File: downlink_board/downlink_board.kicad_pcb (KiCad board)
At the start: 2 copper layers, 65 x 56 mm, 56 parts, among them J1 USB_C_Receptacle_USB2.0, J2 SCREEN, J3 GPIO, J4 PROGRAM, SW1 RPi_{ON}, SW2 RPi_{OFF}, SW3 MCU_{RST}, U1 AZ1117-3.3, U2 TPS563208DDCR, U3 STM32F103C8Tx, U4 nRF24L01, Y1 8M

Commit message: Completed Rev 1.0 layout
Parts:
- removed the C2 at (-5.35, 80.5)
- BT1: moved to F.Cu
- C1: value 22u -> 10u
- C3: renamed from C4; value 22u -> 100n; footprint Capacitor_SMD:C_0805_2012Metric -> Capacitor_SMD:C_0603_1608Metric
- J4: footprint Connector_PinSocket_2.54mm:PinSocket_1x03_P2.54mm_Vertical -> Connector_PinHeader_2.54mm:PinHeader_1x03_P2.54mm_Vertical
- moved R6 155.4 mm to (128.5, 72.2)
- moved U2 154.4 mm to (124.0, 72.2), turned to 0 degrees
- moved R7 148.9 mm to (127.0, 72.2)
- moved R5 148.3 mm to (124.0, 74.8), turned to 0 degrees
- moved C5 136.3 mm to (124.5, 69.5), turned to 180 degrees
- moved JP1 129.9 mm to (154.2, 75.0), turned to 180 degrees
- moved L1 128.9 mm to (111.6, 69.7), turned to 90 degrees
- moved C3 126.7 mm to (118.1, 72.2)
- moved D2 125.1 mm to (107.0, 68.1), turned to 90 degrees
- moved U4 123.0 mm to (125.2, 58.2), turned to 0 degrees
- moved U1 121.5 mm to (151.5, 84.5)
- moved C1 118.8 mm to (116.2, 72.2)
- moved C7 116.7 mm to (116.6, 67.2), turned to 180 degrees
- moved C4 116.2 mm to (146.0, 82.8), turned to -90 degrees
- moved R10 115.6 mm to (107.0, 71.7), turned to 90 degrees
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- renumbered C11 to C10, C12 to C11, C13 to C12, C14 to C13, C15 to C14, C16 to C15, C3 to C2, C5 to C4, C6 to C5, C7 to C6, C8 to C7, C9 to C8, C10 to C9
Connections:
- U3 pad 10: /BATT_{DIV} -> unconnected-(U3-PA0-Pad10)
- U3 pad 12: unconnected-(U3-PA2-Pad12) -> /RF_{EN}
- U3 pad 13: unconnected-(U3-PA3-Pad13) -> /RF_{SEL}
- U3 pad 14: /RF_{INT} -> unconnected-(U3-PA4-Pad14)
- U3 pad 18: /RF_{SEL} -> /RF_{INT}
- U3 pad 19: /RF_{EN} -> /BATT_{DIV}
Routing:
- net /GPIO26: track 0.00 -> 94.5 mm
- net /RST_{MCU}: track 0.00 -> 63.9 mm, vias 0 -> 1
- net /SCL: track 0.00 -> 60.5 mm
- net /RPi_{TX}: track 0.00 -> 51.7 mm, vias 0 -> 3
- net /RPi_{RX}: track 0.00 -> 43.0 mm, vias 0 -> 3
- net /USB_D-: track 0.00 -> 26.9 mm
- net /USB_D+: track 0.00 -> 26.9 mm
- net /BATT_{DIV}: track 0.00 -> 23.9 mm, vias 0 -> 2
- net /STATUS_{3}: track 0.00 -> 19.0 mm, vias 0 -> 2
- net Net-(U1-VI): track 0.00 -> 18.8 mm
- net Net-(JP1-A): track 0.00 -> 18.6 mm
- net /RF_{EN}: track 0.00 -> 17.3 mm
- net unconnected-(J1-SHIELD-PadS1): track 0.00 -> 17.0 mm
- net /MISO: track 0.00 -> 16.9 mm, vias 0 -> 1
- net +3.3V: track 0.00 -> 16.0 mm, vias 0 -> 5
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- added copper zone on B.Cu, net +3.3V
- added copper zone on F.Cu, net +5V
- added copper zone on F.Cu, net +BATT
- added copper zone on F.Cu, net GND
- added copper zone on B.Cu, net Net-(U2-SW)
- added copper zone on F.Cu, net Net-(U2-SW)
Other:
- board text added: "+BATT COVERS THIS TEXT"
- board text added: "3V3"
- board text added: "5V"
- board text added: "5V ON"
- board text added: "BOOT0"
- board text added: "GND"
- board text added: "GND COVERS THIS TEXT"
- board text added: "HPVDT GENERAL DOWNLINK"
- board text added: "MCU RST"
- board text added: "MEANT FOR TOUCHSCREEN"
- board text added: "ONLY CONNECT USB PWR WHEN RPi IS ABSENT!!"
- board text added: "R: ${REVISION}"
- board text added: "RPi OFF"
- board text added: "RPi ON"
- board text added: "SCL"
- board text added: "SDA"
- board text added: "STAT1"
- board text added: "STAT2"
- board text added: "STAT3"
- board text added: "SWCLK"
- board text added: "SWDIO"
- board text added: "The voltage regulator layout is a bit wonky but it's following TI recommendations"
- board text added: "USB PWR"
- board text added: "nRF24L01 COVER THIS"

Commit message: Layout Rev 1.1
Added a keepout area under where the antenna header will go to ensure that if it scratches the board no shorts will occur.
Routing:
- net /STATUS_{3}: track 19.0 -> 20.4 mm
- net /STATUS_{2}: track 15.1 -> 16.1 mm
- net /STATUS_{1}: track 12.2 -> 12.9 mm
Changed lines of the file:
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@@
     (title "Downlink")
     (date "2023-12-05")
-    (rev "1.0")
+    (rev "1.1")
     (company "HPVDT")
     (comment 1 "Common downlink board")
@@
     (effects (font (size 2 2) (thickness 0.15)))
   )
-  (gr_text "The voltage regulator layout is a bit wonky but it's following TI recommendations" (at 101.4 107.6) (layer "User.1")
+  (gr_text "The voltage regulator layout is a bit wonky but it's following TI recommendations" (at 101.4 107.6) (layer "Cmts.User")
     (effects (font (size 1 1) (thickness 0.15)) (justify left bottom))
   )
@@
       (effects (font (size 1 1) (thickness 0.15)) (justify left top mirror))
   )
+  (gr_text_box "Prevent scratches from antenna shorting things"
+    (start 154.5 57.4) (end 165 66.4) (layer "Cmts.User")
+      (effects (font (size 1 1) (thickness 0.15) italic) (justify left top))
+  )
   (segment (start 110.91 55.16) (end 111 55.25) (width 0.25) (layer "B.Cu") (net 2))
   (segment (start 110.91 48.77) (end 110.91 55.16) (width 0.25) (layer "B.Cu") (net 2))
@@
   (segment (start 128.75 74.75) (end 134 69.5) (width 0.25) (layer "B.Cu") (net 15))
   (segment (start 157.25 74.675) (end 157.25 73.1875) (width 0.25) (layer "F.Cu") (net 16))
+  (segment (start 150.6 64.2) (end 150.2 63.8) (width 0.25) (layer "F.Cu") (net 17))
   (segment (start 148.6625 63.25) (end 149.65 63.25) (width 0.25) (layer "F.Cu") (net 17))
-  (segment (start 149.65 63.25) (end 151.2 64.8) (width 0.25) (layer "F.Cu") (net 17))
-  (via (at 151.2 64.8) (size 0.8) (drill 0.4) (layers "F.Cu" "B.Cu") (net 17))
+  (segment (start 149.65 63.25) (end 150.2 63.8) (width 0.25) (layer "F.Cu") (net 17))
+  (segment (start 150.6 65.8) (end 150.6 64.2) (width 0.25) (layer "F.Cu") (net 17))
   (via (at 157.25 71.3125) (size 0.8) (drill 0.4) (layers "F.Cu" "B.Cu") (net 17))
-  (segment (start 157.25 70.85) (end 157.25 71.3125) (width 0.25) (layer "B.Cu") (net 17))
-  (segment (start 151.2 64.8) (end 157.25 70.85) (width 0.25) (layer "B.Cu") (net 17))
+  (via (at 150.6 65.8) (size 0.8) (drill 0.4) (layers "F.Cu" "B.Cu") (net 17))
+  (segment (start 157.25 71.3125) (end 156.1125 71.3125) (width 0.25) (layer "B.Cu") (net 17))
+  (segment (start 156.1125 71.3125) (end 150.6 65.8) (width 0.25) (layer "B.Cu") (net 17))
   (segment (start 107 70.85) (end 107 69.085) (width 0.25) (layer "F.Cu") (net 18))
-  (segment (start 150.376996 62.75) (end 152.426996 64.8) (width 0.25) (layer "F.Cu") (net 19))
+  (segment (start 151.4 63.773004) (end 150.376996 62.75) (width 0.25) (layer "F.Cu") (net 19))
   (segment (start 148.6625 62.75) (end 150.376996 62.75) (width 0.25) (layer "F.Cu") (net 19))
+  (segment (start 151.4 65) (end 151.4 63.773004) (width 0.25) (layer "F.Cu") (net 19))
   (via (at 160.25 71.3125) (size 0.8) (drill 0.4) (layers "F.Cu" "B.Cu") (net 19))
-  (via (at 152.426996 64.8) (size 0.8) (drill 0.4) (layers "F.Cu" "B.Cu") (net 19))
-  (segment (start 153.7375 64.8) (end 160.25 71.3125) (width 0.25) (layer "B.Cu") (net 19))
-  (segment (start 152.426996 64.8) (end 153.7375 64.8) (width 0.25) (layer "B.Cu") (net 19))
+  (via (at 151.4 65) (size 0.8) (drill 0.4) (layers "F.Cu" "B.Cu") (net 19))
+  (segment (start 156.4 70.4) (end 151.4 65.4) (width 0.25) (layer "B.Cu") (net 19))
+  (segment (start 159 71.3125) (end 158.0875 70.4) (width 0.25) (layer "B.Cu") (net 19))
+  (segment (start 158.939496 71.3125) (end 159 71.3125) (width 0.25) (layer "B.Cu") (net 19))
+  (segment (start 159 71.3125) (end 160.25 71.3125) (width 0.25) (layer "B.Cu") (net 19))
+  (segment (start 151.4 65.4) (end 151.4 65) (width 0.25) (layer "B.Cu") (net 19))
+  (segment (start 158.0875 70.4) (end 156.4 70.4) (width 0.25) (layer "B.Cu") (net 19))
   (segment (start 160.25 74.675) (end 160.25 73.1875) (width 0.25) (layer "F.Cu") (net 20))
   (segment (start 148.6625 61.75) (end 150.176996 61.75) (width 0.25) (layer "F.Cu") (net 21))
+  (segment (start 150.501996 61.425) (end 151.498004 61.425) (width 0.25) (layer "F.Cu") (net 21))
+  (segment (start 152.2 62.126996) (end 152.2 64.2) (width 0.25) (layer "F.Cu") (net 21))
+  (segment (start 151.498004 61.425) (end 152.2 62.126996) (width 0.25) (layer "F.Cu") (net 21))
   (segment (start 150.176996 61.75) (end 150.501996 61.425) (width 0.25) (layer "F.Cu") (net 21))
-  (segment (start 150.501996 61.425) (end 153.825 61.425) (width 0.25) (layer "F.Cu") (net 21))
-  (segment (start 153.825 61.425) (end 157.2 64.8) (width 0.25) (layer "F.Cu") (net 21))
-  (via (at 157.2 64.8) (size 0.8) (drill 0.4) (layers "F.Cu" "B.Cu") (net 21))
+  (via (at 152.2 64.2) (size 0.8) (drill 0.4) (layers "F.Cu" "B.Cu") (net 21))
   (via (at 163.0255 71.3125) (size 0.8) (drill 0.4) (layers "F.Cu" "B.Cu") (net 21))
-  (segment (start 157.2 64.8) (end 163.0255 70.6255) (width 0.25) (layer "B.Cu") (net 21))
-  (segment (start 163.0255 70.6255) (end 163.0255 71.3125) (width 0.25) (layer "B.Cu") (net 21))
+  (segment (start 152.2 65.2) (end 152.2 64.2) (width 0.25) (layer "B.Cu") (net 21))
+  (segment (start 160.2 69.8) (end 156.8 69.8) (width 0.25) (layer "B.Cu") (net 21))
+  (segment (start 163.0255 71.3125) (end 161.7125 71.3125) (width 0.25) (layer "B.Cu") (net 21))
+  (segment (start 161.7125 71.3125) (end 160.2 69.8) (width 0.25) (layer "B.Cu") (net 21))
+  (segment (start 156.8 69.8) (end 152.2 65.2) (width 0.25) (layer "B.Cu") (net 21))
   (segment (start 144.75 67.1625) (end 144.75 65.85) (width 0.25) (layer "F.Cu") (net 22))
   (segment (start 142.6 50.2) (end 142.6 52.8) (width 0.25) (layer "F.Cu") (net 22))
@@
   (segment (start 144.25 60.25) (end 145.8 61.8) (width 0.25) (layer "F.Cu") (net 32))
   (via (at 145.8 61.8) (size 0.8) (drill 0.4) (layers "F.Cu" "B.Cu") (net 32))
+  (segment (start 145.8 61.8) (end 146.875 62.875) (width 0.25) (layer "B.Cu") (net 32))
   (segment (start 161.75 92.25) (end 157.5 92.25) (width 0.25) (layer "B.Cu") (net 32))
-  (segment (start 163.75 90.25) (end 161.75 92.25) (width 0.25) (layer "B.Cu") (net 32))
-  (segment (start 147.75 63.75) (end 158.25 63.75) (width 0.25) (layer "B.Cu") (net 32))
+  (segment (start 146.875 62.875) (end 157.375 62.875) (width 0.25) (layer "B.Cu") (net 32))
+  (segment (start 157.375 62.875) (end 163.75 69.25) (width 0.25) (layer "B.Cu") (net 32))
   (segment (start 163.75 69.25) (end 163.75 90.25) (width 0.25) (layer "B.Cu") (net 32))
   (segment (start 157.5 92.25) (end 156 93.75) (width 0.25) (layer "B.Cu") (net 32))
-  (segment (start 145.8 61.8) (end 147.75 63.75) (width 0.25) (layer "B.Cu") (net 32))
   (segment (start 149.5 93.75) (end 156 93.75) (width 0.25) (layer "B.Cu") (net 32))
-  (segment (start 158.25 63.75) (end 163.75 69.25) (width 0.25) (layer "B.Cu") (net 32))
+  (segment (start 163.75 90.25) (end 161.75 92.25) (width 0.25) (layer "B.Cu") (net 32))
   (segment (start 145 87.851166) (end 144.875 87.726166) (width 0.4) (layer "F.Cu") (net 33))
   (segment (start 144.45 92.19) (end 145 91.64) (width 0.4) (layer "F.Cu") (net 33))
@@
       )
     )
+  )
+  (zone (net 0) (net_name "") (layer "F.Cu") (name "ANTENNA") (hatch edge 0.5)
+    (connect_pads (clearance 0))
+    (min_thickness 0.25) (filled_areas_thickness no)
+    (keepout (tracks not_allowed) (vias not_allowed) (pads not_allowed) (copperpour not_allowed) (footprints allowed))
+    (fill (thermal_gap 0.5) (thermal_bridge_width 0.5))
+    (polygon
+      (pts
+        (xy 153.2 54.2)
+        (xy 165 54.2)
+        (xy 165 70.4)
+        (xy 153.2 70.4)
+      )
+    )

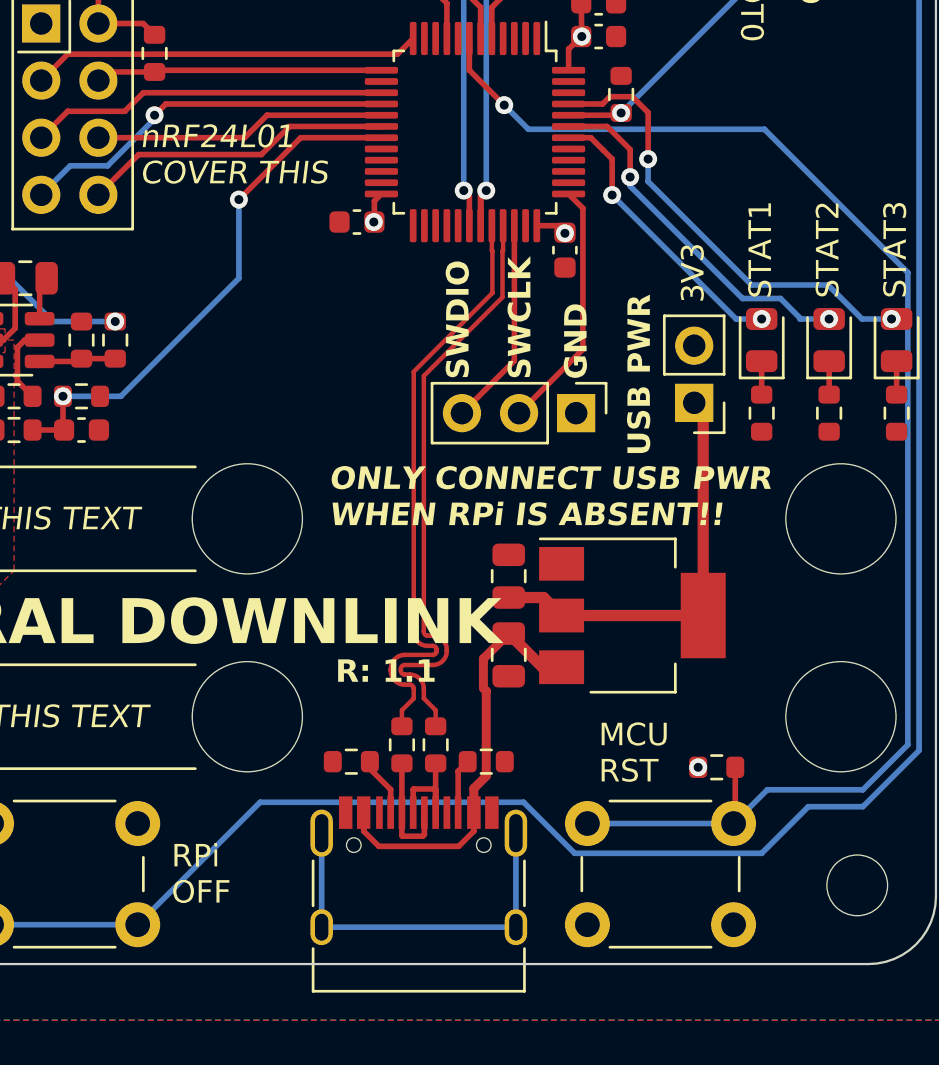
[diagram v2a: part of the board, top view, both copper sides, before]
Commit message: Layout V1.2, no more USB overhang
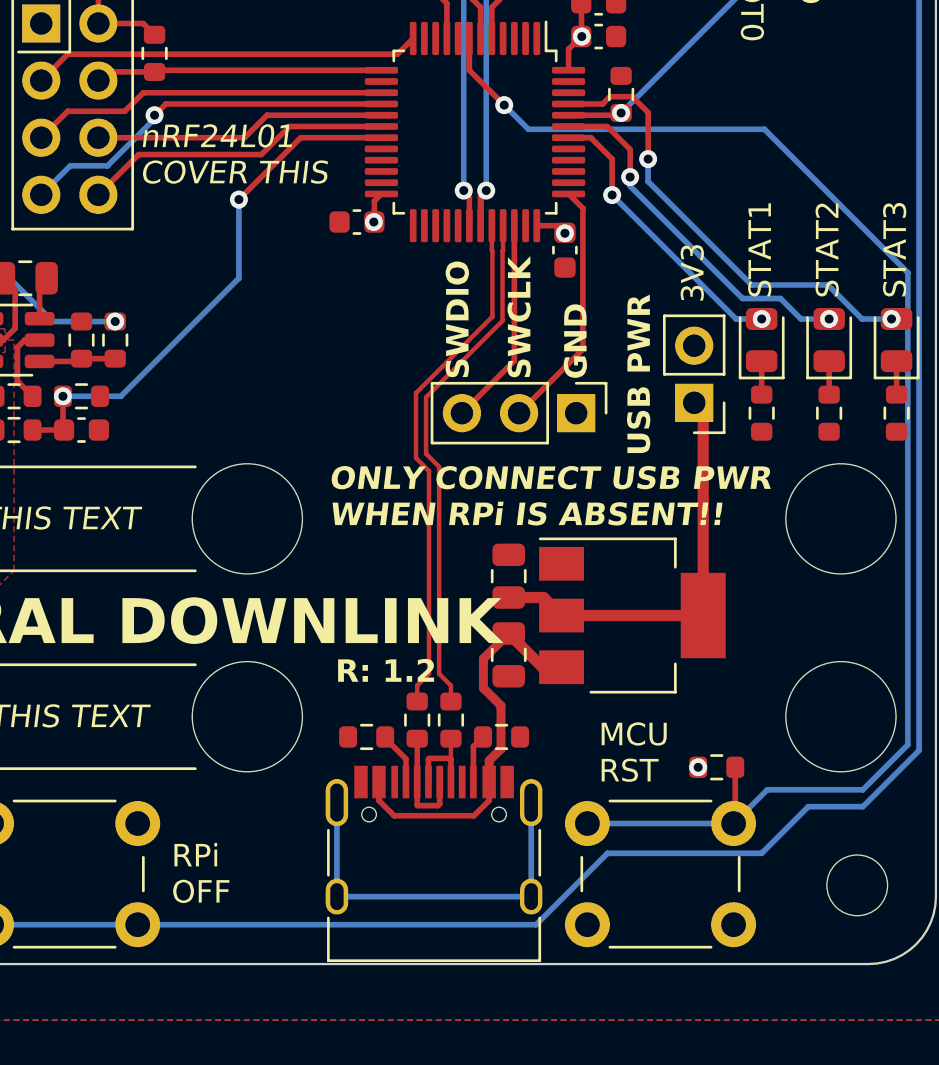
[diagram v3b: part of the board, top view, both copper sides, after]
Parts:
- moved J1 1.52 mm to (142.7, 96.0)
- moved R1 1.29 mm to (139.7, 89.9)
- moved R2 1.29 mm to (145.7, 89.9)
- moved R3 1.29 mm to (141.9, 89.2)
- moved R4 1.29 mm to (143.4, 89.2)
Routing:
- net /USB_D-: track 26.9 -> 23.0 mm
- net /USB_D+: track 26.9 -> 23.0 mm
- net /GPIO26: track 94.5 -> 92.7 mm
- net Net-(U1-VI): track 18.8 -> 17.7 mm
